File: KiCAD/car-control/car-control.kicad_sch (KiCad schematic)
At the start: 24 parts, among them J1 Conn_02x03_Odd_Even, J2 Conn_01x06, SW1 SW_Push, SW2 COM-15140, SW2 SW_Push, SW3 SW_Push, SW4 SW_Push, U3 ATmega328-P

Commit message: working on PCB
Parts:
- removed C1: 0.1uF, Capacitor_SMD:C_1206_3216Metric_Pad1.33x1.80mm_HandSolder, symbol Device:C
- removed DS1: RC1602A, Display:WC1602A, symbol Display_Character:RC1602A
- removed R2: 470, Resistor_SMD:R_1206_3216Metric_Pad1.30x1.75mm_HandSolder, symbol Device:R
- removed RV1: 10k, Potentiometer_THT:Potentiometer_Bourns_3266W_Vertical, symbol Device:R_Potentiometer
- removed U3: ATmega328-P, Package_DIP:DIP-28_W7.62mm, symbol MCU_Microchip_ATmega:ATmega328-P
- added A1: Arduino_MKR_Zero_Socket, PCM_arduino-library:Arduino_MKR_Zero_Socket, symbol arduino-library:Arduino_MKR_Zero_Socket
- added U1: OLED-SSD1322, symbol my_oled:oled_16p
- renumbered SW2 to SW5
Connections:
- net GND: now also U1.1 (GND), U1.14 (E)
- new net +3.3V: U1.2 (VCC)
- no-connect marks 0 -> 6

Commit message: working on layout
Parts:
- removed J1: Conn_02x03_Odd_Even, Connector_PinHeader_2.54mm:PinHeader_2x03_P2.54mm_Vertical, symbol Connector_Generic:Conn_02x03_Odd_Even
- added J1: USB_B_Micro, my_USB:CONN_USB3131-30-0230-A_GCT, symbol Connector:USB_B_Micro
- added J3: USB_A, my_USB:CONN_USB-A-S-VT_ADM, symbol Connector:USB_A
- added J4: Conn_01x04, Connector_PinSocket_2.54mm:PinSocket_1x04_P2.54mm_Vertical, symbol Connector_Generic:Conn_01x04
- added R2: 10k, Resistor_SMD:R_1206_3216Metric_Pad1.30x1.75mm_HandSolder, symbol Device:R
- R1: CatNo 311-10.0KFRCT-ND -> (none); MfgNo RC1206FR-0710KL -> (none)
- R3, R4: value 3.3k -> 1k
- U1: footprint (none) -> my_OLED:OLED_312_16pin
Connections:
- net RXD is gone; now on net GND: J2.2 (Pin_2)
- net TXD is gone; now on net A1: J2.3 (Pin_3)
- net nCTS is gone; now on net +3.3V: J2.5 (Pin_5)
- net nDTR is gone; now on net A0: J2.1 (Pin_1)
- net nRST is gone; now on net A0: R1.2
- net +3.3V: now also A1.3V3 (3.3V), R1.1, R3.1, R4.1, J4.1 (Pin_1), R2.1
- net ENC_A: now also A1.D12 (D12/SCL)
- net ENC_B: now also A1.D11 (D11/SDA)
- net ENC_GRN: now also A1.D1
- net ENC_RED: now also A1.D2
- net ENC_SW: now also A1.D3
- net GND: now also A1.GND, J2.4 (Pin_4), J1.5 (GND), J1.6 (Shield), J3.4 (GND), J3.5 (Shield), J4.4 (Pin_4)
- net MISO: now also A1.D10 (D10_MISO)
- net MOSI: now also A1.D8 (D8_MOSI), U1.7 (SCLK)
- net SCK: now also A1.D9 (D9_SCK), U1.8 (SDA)
- net SW0: now also A1.A6
- net SW1: now also A1.A5
- net SW2: now also A1.A4
- net SW3: now also A1.A3
- net LED1: now reaches D2.1 (K)
- net LED1: now also A1.D0
- net LED0: now reaches D1.1 (K)
- net LED0: now also A1.A2
- net ~{CS}: now reaches U1.15 (~{CS})
- net ~{CS}: now also A1.D4
- net ~{RST}: now reaches U1.16 (~{RST})
- net ~{RST}: now also A1.D6
- net DC: now reaches U1.4 (DC)
- net DC: now also A1.D5
- net A0: now reaches A1.A0 (A0/DAC)
- net A1: now reaches A1.A1
- net A1: now also R2.2
- net RX: now reaches A1.D13 (D13/RX)
- net RX: now also J4.2 (Pin_2)
- net TX: now reaches A1.D14 (D14/TX)
- net TX: now also J4.3 (Pin_3)
- removed net VCC: J2.4 (Pin_4), R1.1, R3.1, R4.1
- new net: J1.1 (VBUS), J3.1 (VBUS)
- new net: J1.2 (D-), J3.2 (D-)
- new net: J1.3 (D+), J3.3 (D+)
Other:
- note added: "Analog sensors"
- note added: "Car Computer V1.0 Control Panel"
- note added: "GPS"
- note added: "USB Feed-thru"
- note removed: "Generic Control Panel Boston University EPIC"
- moved on the sheet: A1, D1, D2, H1, H2, H3, H4, J2, N1, R3, R4, SW1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

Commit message: PCB done?
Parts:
- added JP1: Jumper_3_Bridged12, Connector_PinHeader_2.54mm:PinHeader_1x03_P2.54mm_Vertical, symbol Jumper:Jumper_3_Bridged12
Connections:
- net +3.3V: no longer J4.1 (Pin_1)
- net VBUS: now reaches J1.1 (VBUS), J3.1 (VBUS)
- net VBUS: now also JP1.3 (B)
- net +5V: now reaches A1.5V
- net +5V: now also JP1.1 (A)
- new net: J4.1 (Pin_1), JP1.2 (C)
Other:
- moved on the sheet: J4

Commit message: updates to case
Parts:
- R1, R2, R3, R4, R5, R6: now left out of the parts list
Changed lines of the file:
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@@
 		(unit 1)
 		(exclude_from_sim no)
-		(in_bom yes)
+		(in_bom no)
 		(on_board yes)
 		(dnp no)
@@
 		(unit 1)
 		(exclude_from_sim no)
-		(in_bom yes)
+		(in_bom no)
 		(on_board yes)
 		(dnp no)
@@
 		(unit 1)
 		(exclude_from_sim no)
-		(in_bom yes)
+		(in_bom no)
 		(on_board yes)
 		(dnp no)
@@
 		(unit 1)
 		(exclude_from_sim no)
-		(in_bom yes)
+		(in_bom no)
 		(on_board yes)
 		(dnp no)
@@
 		(unit 1)
 		(exclude_from_sim no)
-		(in_bom yes)
+		(in_bom no)
 		(on_board yes)
 		(dnp no)
@@
 		(unit 1)
 		(exclude_from_sim no)
-		(in_bom yes)
-		(on_board yes)
-		(dnp no)
+		(in_bom no)
+		(on_board yes)
+		(dnp no)

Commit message: initial software, fix layout
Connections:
- net DC: now also U1.14 (DC); no longer U1.4 (DC)
- net GND: now also U1.10 (D6), U1.11 (D7), U1.12 (RD), U1.13 (WR), U1.7 (D3), U1.8 (D4), U1.9 (D5); no longer U1.14 (E)
- net MOSI: now also U1.5 (D1/SDA); no longer U1.7 (SCLK)
- net SCK: now also U1.4 (D0/SCK); no longer U1.8 (SDA)
- net MISO: no longer names the net of A1.D10 (D10_MISO)
- no-connect marks 6 -> 2

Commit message: PCB V1.0 as built
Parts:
- J4: footprint Connector_PinSocket_2.54mm:PinSocket_1x04_P2.54mm_Vertical -> Connector_PinSocket_2.54mm:PinSocket_1x05_P2.54mm_Vertical; symbol Connector_Generic:Conn_01x04 -> Connector_Generic:Conn_01x05
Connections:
- net GND: now also J4.2 (Pin_2); no longer J4.4 (Pin_4)
- net RX: now also J4.3 (Pin_3); no longer J4.2 (Pin_2)
- net TX: now also J4.4 (Pin_4); no longer J4.3 (Pin_3)
- no-connect marks 2 -> 3
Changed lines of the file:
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@@
+	)
+	(no_connect
+		(at 134.62 116.84)
 	)
 	(no_connect
@@
 	(wire
 		(pts
-			(xy 116.84 109.22) (xy 125.73 109.22)
+			(xy 125.73 111.76) (xy 134.62 111.76)
 		)
 		(stroke
@@
 	(wire
 		(pts
-			(xy 125.73 106.68) (xy 123.19 106.68)
+			(xy 123.19 106.68) (xy 134.62 106.68)
 		)
 		(stroke
@@
 	(wire
 		(pts
-			(xy 116.84 111.76) (xy 125.73 111.76)
+			(xy 125.73 114.3) (xy 134.62 114.3)
 		)
 		(stroke
@@
 	(wire
 		(pts
-			(xy 123.19 114.3) (xy 123.19 118.11)
+			(xy 118.11 109.22) (xy 118.11 113.03)
 		)
 		(stroke
@@
 	(wire
 		(pts
-			(xy 125.73 114.3) (xy 123.19 114.3)
+			(xy 118.11 109.22) (xy 134.62 109.22)
 		)
 		(stroke
@@
 	)
 	(label "RX"
-		(at 119.38 109.22 0)
+		(at 128.27 111.76 0)
 		(effects
 			(font
@@
 	)
 	(label "TX"
-		(at 119.38 111.76 0)
+		(at 128.27 114.3 0)
 		(effects
 			(font
@@
 	(symbol
 		(lib_id "power:GND")
-		(at 123.19 118.11 0)
+		(at 118.11 113.03 0)
 		(unit 1)
 		(exclude_from_sim no)
@@
 		(fields_autoplaced yes)
 		(property "Reference" "#PWR014"
-			(at 123.19 124.46 0)
+			(at 118.11 119.38 0)
 			(effects
 				(font
@@
 		)
 		(property "Value" "GND"
-			(at 123.19 123.19 0)
+			(at 118.11 118.11 0)
 			(effects
 				(font
@@
 		)
 		(property "Footprint" ""
-			(at 123.19 118.11 0)
+			(at 118.11 113.03 0)
 			(effects
 				(font
@@
 		)
 		(property "Datasheet" ""
-			(at 123.19 118.11 0)
+			(at 118.11 113.03 0)
 			(effects
 				(font
@@
 		)
 		(property "Description" ""
-			(at 123.19 118.11 0)
+			(at 118.11 113.03 0)
 			(effects
 				(font
@@
 	)
 	(symbol
-		(lib_id "Connector_Generic:Conn_01x04")
-		(at 130.81 109.22 0)
+		(lib_id "Connector_Generic:Conn_01x05")
+		(at 139.7 111.76 0)
 		(unit 1)
 		(exclude_from_sim no)
@@
 		(fields_autoplaced yes)
 		(property "Reference" "J4"
-			(at 133.35 109.2199 0)
+			(at 142.24 110.4899 0)
 			(effects
 				(font
@@
 		)
 		(property "Value" "Conn_01x04"
-			(at 133.35 111.7599 0)
+			(at 142.24 113.0299 0)
 			(effects
 				(font
@@
 			)
 		)
-		(property "Footprint" "Connector_PinSocket_2.54mm:PinSocket_1x04_P2.54mm_Vertical"
-			(at 130.81 109.22 0)
+		(property "Footprint" "Connector_PinSocket_2.54mm:PinSocket_1x05_P2.54mm_Vertical"
+			(at 139.7 111.76 0)
 			(effects
 				(font
@@
 		)
 		(property "Datasheet" "~"
-			(at 130.81 109.22 0)
-			(effects
-				(font
-					(size 1.27 1.27)
-				)
-				(hide yes)
-			)
-		)
-		(property "Description" "Generic connector, single row, 01x04, script generated (kicad-library-utils/schlib/autogen/connector/)"
-			(at 130.81 109.22 0)
+			(at 139.7 111.76 0)
+			(effects
+				(font
+					(size 1.27 1.27)
+				)
+				(hide yes)
+			)
+		)
+		(property "Description" "Generic connector, single row, 01x05, script generated (kicad-library-utils/schlib/autogen/connector/)"
+			(at 139.7 111.76 0)
 			(effects
 				(font
@@
 		(pin "3"
 		)
+		(pin "5"
+		)
 		(instances

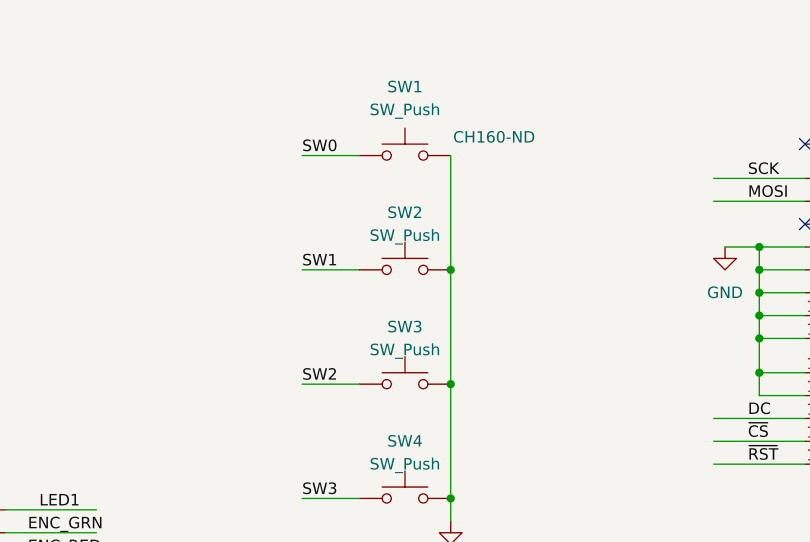
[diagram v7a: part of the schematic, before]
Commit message: update panel and box
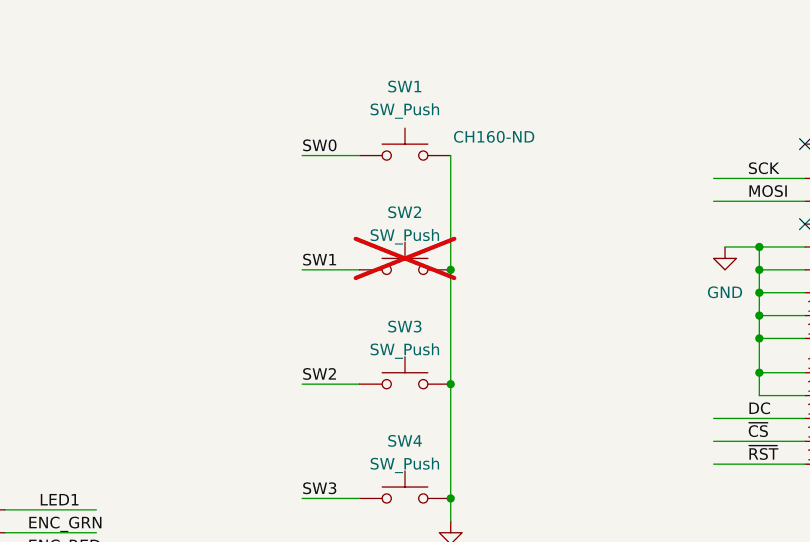
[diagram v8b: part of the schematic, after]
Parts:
- SW2: now not fitted
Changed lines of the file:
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@@
 		(exclude_from_sim no)
 		(in_bom yes)
-		(on_board yes)
+		(on_board no)
 		(dnp no)
 		(fields_autoplaced yes)
@@
 		(in_bom yes)
 		(on_board yes)
-		(dnp no)
+		(dnp yes)
 		(fields_autoplaced yes)
 		(property "Reference" "SW2"
